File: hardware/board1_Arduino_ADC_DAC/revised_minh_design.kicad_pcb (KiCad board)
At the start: 4 copper layers, 96 x 43.9 mm, 40 parts, among them J1 Conn_01x03_Male, J2 Conn_02x08_Odd_Even, J3 Conn_02x08_Odd_Even, J4 Conn_02x08_Odd_Even, J5 Conn_01x02_Male, U1 ESP32-DevKit-C, U2 LM7805_TO220, U3 MCP1754S-3302xCB, U4 MCP1825S-3.3V, U5 MCP1501-33xSN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

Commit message: cleanup
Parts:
- added C19: 10uF, Capacitor_SMD:C_0805_2012Metric_Pad1.18x1.45mm_HandSolder, F.Cu at (137.5, 52.0)
- added C20: 0.1uF, Capacitor_SMD:C_0805_2012Metric_Pad1.18x1.45mm_HandSolder, F.Cu at (137.7, 49.0)
- added C21: 10uF, Capacitor_SMD:C_0805_2012Metric_Pad1.18x1.45mm_HandSolder, F.Cu at (134.3, 57.3)
- added C22: 0.1uF, Capacitor_SMD:C_0805_2012Metric_Pad1.18x1.45mm_HandSolder, F.Cu at (130.6, 58.8)
- added R4: 0, Resistor_SMD:R_0805_2012Metric_Pad1.20x1.40mm_HandSolder, F.Cu at (118.7, 51.3)
- added R5: 100k, Resistor_SMD:R_0805_2012Metric_Pad1.20x1.40mm_HandSolder, F.Cu at (119.9, 43.9)
- added R6: 100k, Resistor_SMD:R_0805_2012Metric_Pad1.20x1.40mm_HandSolder, F.Cu at (114.8, 57.3)
- added TP1: TestPoint, Connector_PinHeader_2.54mm:PinHeader_1x01_P2.54mm_Vertical, F.Cu at (118.2, 55.5)
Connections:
- A1 pad 14: SI -> PI
- A1 pad 15: SO -> PO
- A1 pad 19: MDAT -> MDAT1
- A1 pad 22: unconnected-(A1-Pad22) -> MDAT2
- J4 pad 1: VoutB -> VoutH
- J4 pad 11: VoutE -> VoutC
- J4 pad 13: VoutC -> VoutB
- J4 pad 3: VoutD -> VoutG
- J4 pad 7: VoutH -> VoutE
- J4 pad 9: VoutG -> VoutD
- R3 pad 1: Net-(R3-Pad1) -> ADC_CLK2
- R3 pad 2: CLK -> Net-(X1-Pad3)
- U1 pad 25: MDAT -> MDAT1
- U1 pad 28: unconnected-(U1-Pad28) -> MDAT2
- U1 pad 32: SI -> PI
- U1 pad 34: SO -> PO
- U6 pad 15: SI -> PI
- U6 pad 16: SO -> PO
- U6 pad 17: MDAT -> MDAT1
- U6 pad 18: CLK -> ADC_CLK1
- U7 pad 15: SI -> PI
- U7 pad 16: SO -> PO
- U7 pad 17: MDAT -> MDAT2
- U7 pad 18: CLK -> ADC_CLK2
- U8 pad 15: SO -> PI
- X1 pad 3: Net-(R3-Pad1) -> Net-(X1-Pad3)
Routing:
- net SO: track 114.4 -> 0.00 mm
- net PI: track 0.00 -> 109.0 mm
- net PO: track 0.00 -> 91.5 mm
- net MDAT1: track 0.00 -> 90.8 mm, vias 0 -> 4
- net SI: track 85.6 -> 0.00 mm
- net MDAT: track 75.7 -> 0.00 mm, vias 2 -> 0
- net CLK: track 21.6 -> 0.00 mm, vias 2 -> 0
- net ADC2_4: track 13.6 -> 28.8 mm
- net ADC2_3: track 15.3 -> 0.00 mm
- net VoutH: track 5.90 -> 11.1 mm
- net MDAT2: track 0.00 -> 5.10 mm
- net VoutE: track 9.32 -> 5.90 mm
- net VoutC: track 12.5 -> 9.32 mm
- net VoutG: track 6.40 -> 9.08 mm
- net VoutD: track 9.08 -> 6.40 mm
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
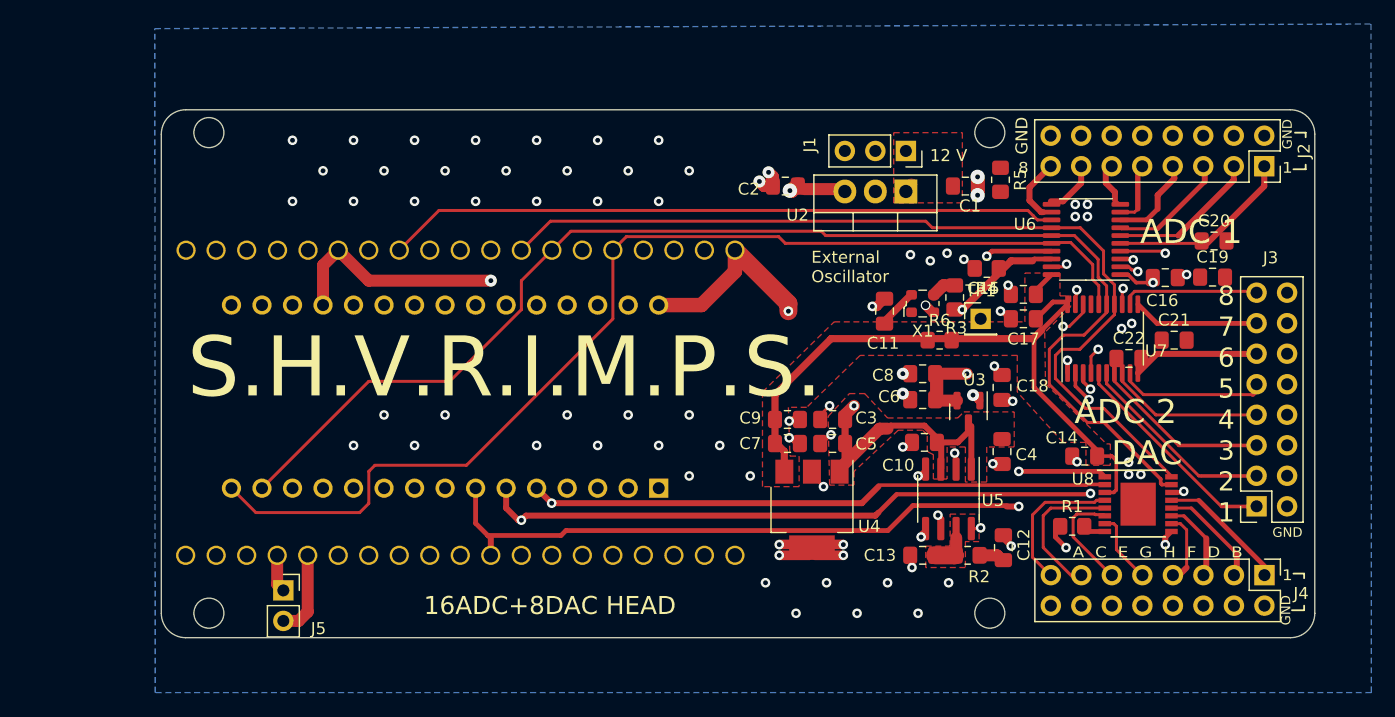
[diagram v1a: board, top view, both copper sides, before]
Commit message: routed the netlist for ADC/DAC v2
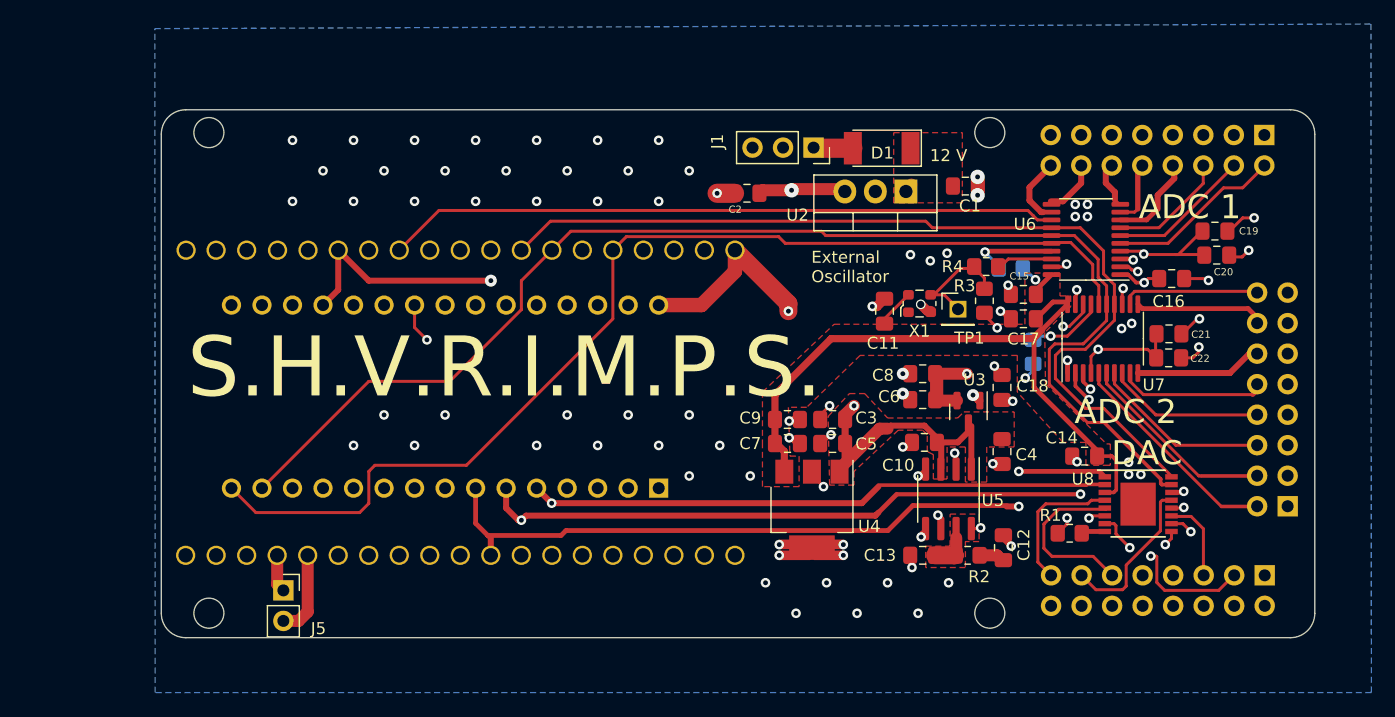
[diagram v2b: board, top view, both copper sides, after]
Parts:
- added D1: SM4004, Diode_SMD:D_MELF, F.Cu at (110.0, 41.3)
- J2, J3, R5, R6: moved to B.Cu
- moved R6 7.84 mm to (122.6, 58.2), turned to 90 degrees
- moved J1 7.69 mm to (104.3, 41.2)
- moved R5 7.42 mm to (120.8, 51.3), turned to 0 degrees
- moved C19 3.84 mm to (137.7, 48.2)
- moved C22 3.31 mm to (133.9, 58.8)
- moved C2 3.25 mm to (98.8, 45.0)
- moved J2 2.60 mm to (141.8, 40.2), turned to 90 degrees
- moved J3 2.59 mm to (143.8, 71.1), turned to 0 degrees
- moved R3 2.49 mm to (118.5, 54.0), turned to 90 degrees
- moved TP1 2.05 mm to (116.3, 54.7)
- moved C20 1.20 mm to (137.9, 50.2)
- moved C21 0.68 mm to (133.9, 56.8)
- moved R1 0.61 mm to (125.7, 73.3)
- moved C16 0.54 mm to (134.1, 52.1)
- moved X1 0.26 mm to (113.2, 54.2)
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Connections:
- J1 pad 1: +12V -> Net-(J1-Pad1)
- J2 pad 1: ADC1_1 -> Earth
- J2 pad 10: Earth -> ADC1_5
- J2 pad 11: ADC1_6 -> Earth
- J2 pad 12: Earth -> ADC1_6
- J2 pad 13: ADC1_7 -> Earth
- J2 pad 14: Earth -> ADC1_7
- J2 pad 15: ADC1_8 -> Earth
- J2 pad 16: Earth -> ADC1_8
- J2 pad 2: Earth -> ADC1_1
- J2 pad 3: ADC1_2 -> Earth
- J2 pad 4: Earth -> ADC1_2
- J2 pad 5: ADC1_3 -> Earth
- J2 pad 6: Earth -> ADC1_3
- J2 pad 7: ADC1_4 -> Earth
- J2 pad 8: Earth -> ADC1_4
- J2 pad 9: ADC1_5 -> Earth
- J3 pad 1: ADC2_1 -> Earth
- J3 pad 10: Earth -> ADC2_5
- J3 pad 11: ADC2_6 -> Earth
- J3 pad 12: Earth -> ADC2_6
- J3 pad 13: ADC2_7 -> Earth
- J3 pad 14: Earth -> ADC2_7
- J3 pad 15: ADC2_8 -> Earth
- J3 pad 16: Earth -> ADC2_8
- J3 pad 2: Earth -> ADC2_1
- J3 pad 3: ADC2_2 -> Earth
- J3 pad 4: Earth -> ADC2_2
- J3 pad 5: ADC2_3 -> Earth
- J3 pad 6: Earth -> ADC2_3
- J3 pad 7: ADC2_4 -> Earth
- J3 pad 8: Earth -> ADC2_4
- J3 pad 9: ADC2_5 -> Earth
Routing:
- net MDAT2: track 5.10 -> 70.2 mm, vias 0 -> 2
- net MDAT1: track 90.8 -> 71.0 mm, vias 4 -> 2
- net ADC2_4: track 28.8 -> 13.6 mm
- net ADC2_3: track 0.00 -> 14.9 mm
- net VoutE: track 5.90 -> 17.1 mm, vias 0 -> 1
- net +3.3VDAC: track 49.8 -> 59.6 mm
- net Earth: track 46.1 -> 55.2 mm, vias 91 -> 94
- net Net-(R3-Pad2): track 0.00 -> 8.90 mm, vias 1 -> 0
- net ADC_CLK2: track 2.08 -> 10.1 mm, vias 0 -> 2
- net VoutG: track 9.08 -> 15.2 mm, vias 0 -> 2
- net VoutC: track 9.32 -> 14.4 mm
- net ADC_CLK1: track 0.00 -> 4.72 mm
- net +5V: track 62.6 -> 58.7 mm
- net +3V3: track 59.8 -> 62.8 mm, vias 0 -> 2
- net Net-(J1-Pad1): track 0.00 -> 2.41 mm
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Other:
- board text added: "16ADC+8DAC HEAD (v2)"
- board text added: "2"
- board text added: "3"
- board text added: "4"
- board text added: "5"
- board text added: "6"
- board text added: "7"
- board text added: "H G F E D C B A"
- board text removed: "16ADC+8DAC HEAD"
- board text removed: "8 7 6 5 4 3 2 1"
- board text removed: "A C E G H F D B"

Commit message: hardware update to add GPIO directly to MCU
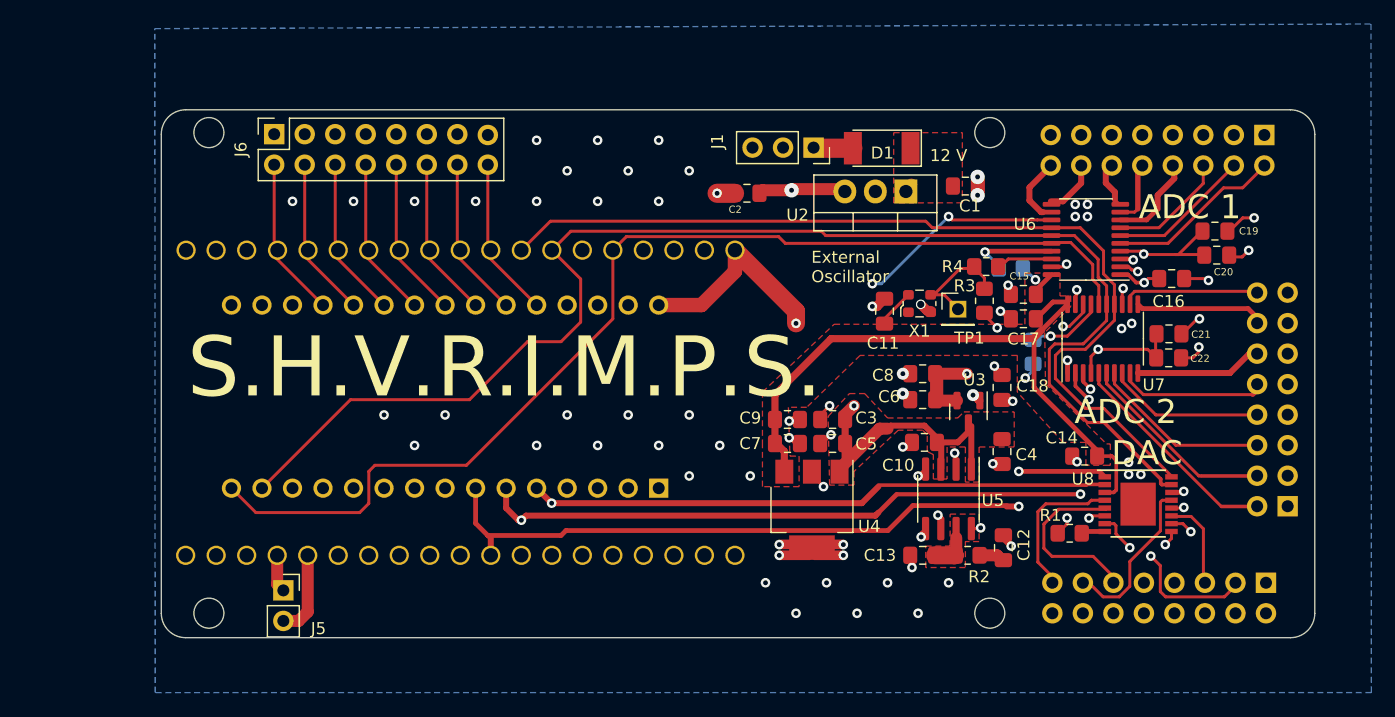
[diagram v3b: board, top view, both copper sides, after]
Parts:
- added J6: Conn_02x08_Odd_Even, Connector_PinSocket_2.54mm:PinSocket_2x08_P2.54mm_Vertical, F.Cu at (59.4, 40.1)
- moved J4 0.63 mm to (142.0, 77.5)
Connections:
- A1 pad 10: unconnected-(A1-Pad10) -> ~{ADC2_CS}
- A1 pad 11: unconnected-(A1-Pad11) -> MDAT1
- A1 pad 19: MDAT1 -> GPIO_0
- A1 pad 20: ~{ADC2_CS} -> GPIO_1
- A1 pad 21: ~{ADC1_CS} -> GPIO_2
- A1 pad 22: MDAT2 -> GPIO_3
- A1 pad 23: unconnected-(A1-Pad23) -> GPIO_4
- A1 pad 24: unconnected-(A1-Pad24) -> GPIO_5
- A1 pad 25: unconnected-(A1-Pad25) -> GPIO_6
- A1 pad 26: unconnected-(A1-Pad26) -> GPIO_7
- A1 pad 8: unconnected-(A1-Pad8) -> MDAT2
- A1 pad 9: unconnected-(A1-Pad9) -> ~{ADC1_CS}
- U1 pad 10: unconnected-(U1-Pad10) -> MDAT2
- U1 pad 11: unconnected-(U1-Pad11) -> ~{ADC1_CS}
- U1 pad 12: unconnected-(U1-Pad12) -> ~{ADC2_CS}
- U1 pad 14: unconnected-(U1-Pad14) -> MDAT1
- U1 pad 23: unconnected-(U1-Pad23) -> GPIO_0
- U1 pad 24: unconnected-(U1-Pad24) -> GPIO_1
- U1 pad 25: MDAT1 -> GPIO_2
- U1 pad 26: ~{ADC2_CS} -> GPIO_3
- U1 pad 27: ~{ADC1_CS} -> GPIO_4
- U1 pad 28: MDAT2 -> GPIO_5
- U1 pad 29: unconnected-(U1-Pad29) -> GPIO_6
- U1 pad 30: unconnected-(U1-Pad30) -> GPIO_7
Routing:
- net GPIO_7: track 0.00 -> 13.4 mm
- net GPIO_5: track 0.00 -> 13.4 mm
- net GPIO_3: track 0.00 -> 13.4 mm
- net GPIO_1: track 0.00 -> 13.4 mm
- net GPIO_0: track 0.00 -> 13.4 mm
- net GPIO_6: track 0.00 -> 13.4 mm
- net GPIO_4: track 0.00 -> 13.4 mm
- net GPIO_2: track 0.00 -> 13.4 mm
- net MDAT1: track 71.0 -> 80.4 mm, vias 2 -> 1
- net ~{ADC1_CS}: track 61.1 -> 68.6 mm, vias 0 -> 2
- net PI: track 109.4 -> 114.9 mm
- net ~{ADC2_CS}: track 73.9 -> 79.2 mm
- net SK: track 107.1 -> 112.3 mm
- net VoutE: track 17.1 -> 17.9 mm
- net VoutB: track 13.5 -> 14.2 mm
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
